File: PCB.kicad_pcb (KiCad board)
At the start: 2 copper layers, 60 x 60 mm, 56 parts, among them J1 USB_C_Receptacle_USB2.0_16P, J10 Conn_01x05_Pin, J11 Conn_01x05_Pin, J2 Conn_01x04_Pin, J3 Conn_01x04_Pin, J4 Conn_01x07_Pin, J5 Conn_01x02_Pin, J6 Conn_01x02_Pin, J7 Conn_01x02_Pin, J8 Conn_01x04_Pin, J9 Conn_01x07_Pin, SW1 SW_Push, SW2 SW_Push, U1 TMC2209_SILENTSTEPSTICK, U2 TMC2209_SILENTSTEPSTICK, U3 D3V3XA4B10LP, U4 AMS1117-3.3 (UMW), U5 TMC2209_SILENTSTEPSTICK, U6 ESP32-S3-WROOM-1

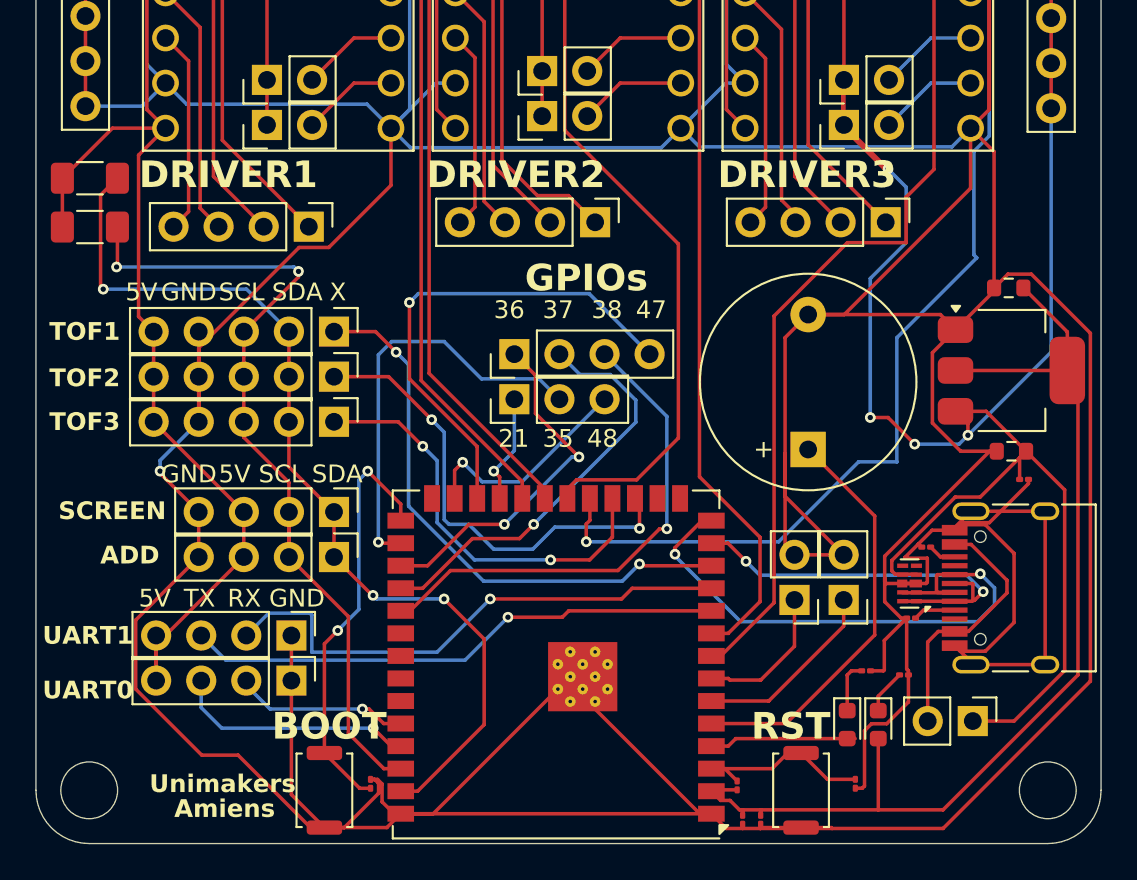
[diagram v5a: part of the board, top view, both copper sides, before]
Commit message: ajout hub 3.3v
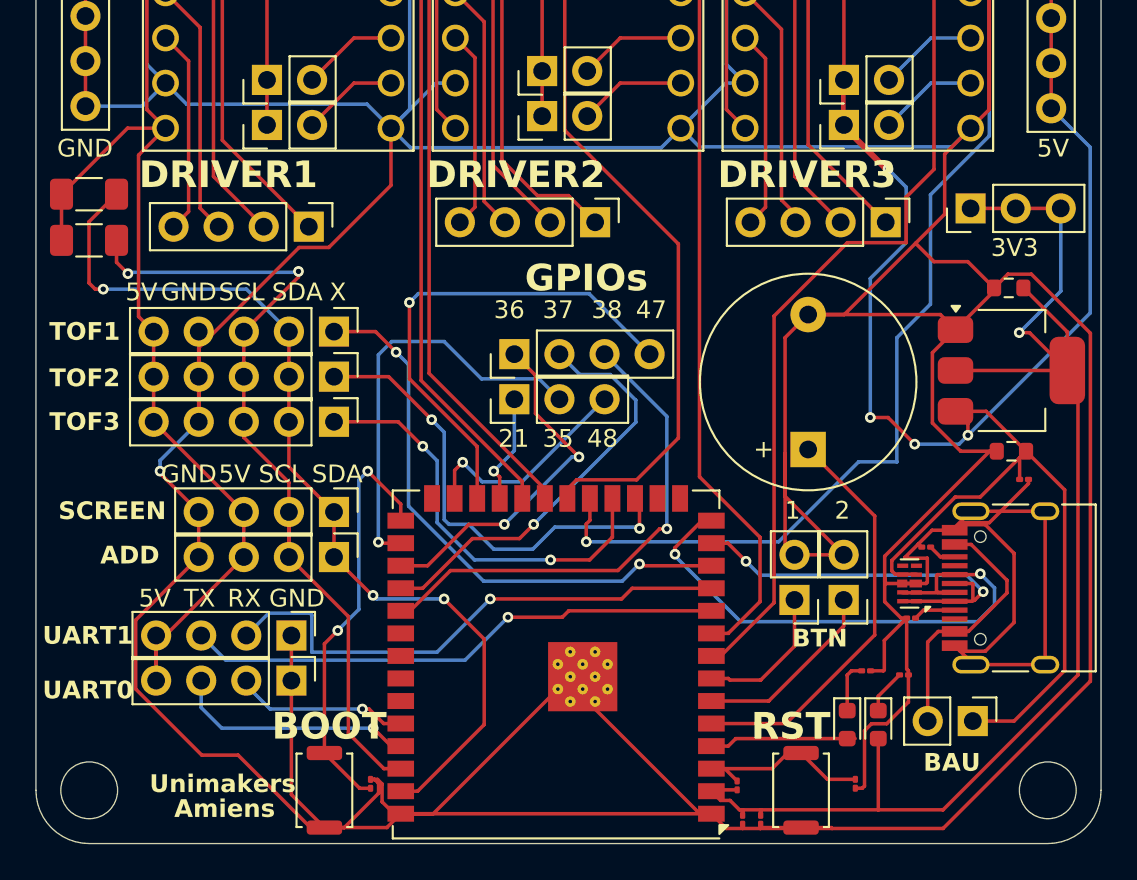
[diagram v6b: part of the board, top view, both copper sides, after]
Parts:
- added J12: Conn_01x03_Pin, Connector_PinHeader_2.54mm:PinHeader_1x03_P2.54mm_Vertical, F.Cu at (162.9, 97.2)
- moved JP8 0.90 mm to (113.2, 96.4)
- moved JP7 0.75 mm to (113.2, 99.0)
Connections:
- J11 pad 1: GND -> unconnected-(J11-Pin_1-Pad1)
- J11 pad 2: GND -> unconnected-(J11-Pin_2-Pad2)
- J11 pad 3: GND -> unconnected-(J11-Pin_3-Pad3)
- J11 pad 4: GND -> unconnected-(J11-Pin_4-Pad4)
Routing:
- net 3V3: track 59.7 -> 76.4 mm, vias 0 -> 1
- net GND: track 583.1 -> 579.0 mm
- net VCC_5V: track 323.5 -> 325.6 mm
- net SCL: track 48.7 -> 47.8 mm
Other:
- board text added: "1"
- board text added: "2"
- board text added: "3V3"
- board text added: "BAU"
- board text added: "BTN"

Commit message: Dernier DRC après modicifications
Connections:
- J11 pad 1: unconnected-(J11-Pin_1-Pad1) -> GND
- J11 pad 2: unconnected-(J11-Pin_2-Pad2) -> GND
- J11 pad 3: unconnected-(J11-Pin_3-Pad3) -> GND
- J11 pad 4: unconnected-(J11-Pin_4-Pad4) -> GND
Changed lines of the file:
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@@
 	(net 75 "MOTORC3")
 	(net 76 "MOTORC2")
-	(net 77 "unconnected-(J11-Pin_4-Pad4)")
-	(net 78 "unconnected-(J11-Pin_3-Pad3)")
-	(net 79 "unconnected-(J11-Pin_1-Pad1)")
-	(net 80 "unconnected-(J11-Pin_2-Pad2)")
 	(footprint "Buzzer_Beeper:Buzzer_12x9.5RM7.6"
 		(layer "F.Cu")
@@
 			(layers "*.Cu" "*.Mask")
 			(remove_unused_layers no)
-			(net 79 "unconnected-(J11-Pin_1-Pad1)")
+			(net 64 "GND")
 			(pinfunction "Pin_1")
 			(pintype "passive")
@@
 			(layers "*.Cu" "*.Mask")
 			(remove_unused_layers no)
-			(net 80 "unconnected-(J11-Pin_2-Pad2)")
+			(net 64 "GND")
 			(pinfunction "Pin_2")
 			(pintype "passive")
@@
 			(layers "*.Cu" "*.Mask")
 			(remove_unused_layers no)
-			(net 78 "unconnected-(J11-Pin_3-Pad3)")
+			(net 64 "GND")
 			(pinfunction "Pin_3")
 			(pintype "passive")
@@
 			(layers "*.Cu" "*.Mask")
 			(remove_unused_layers no)
-			(net 77 "unconnected-(J11-Pin_4-Pad4)")
+			(net 64 "GND")
 			(pinfunction "Pin_4")
 			(pintype "passive")

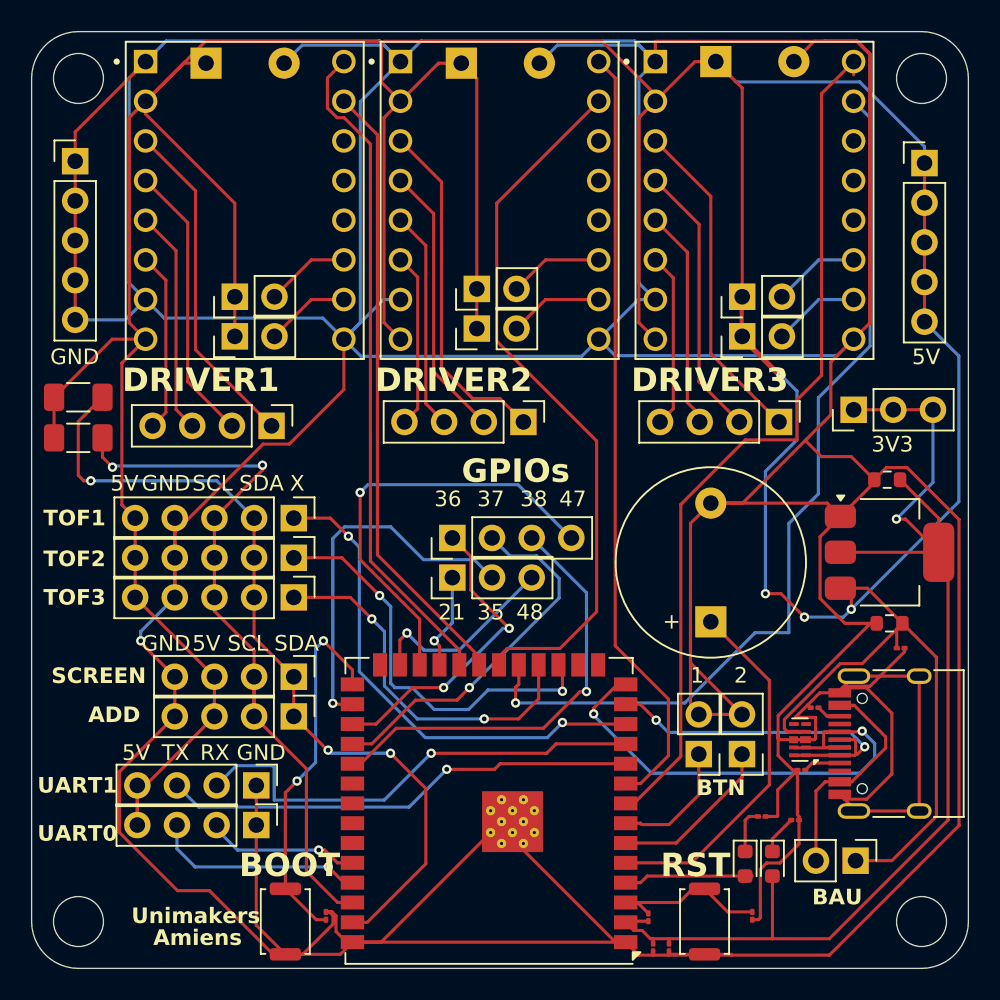
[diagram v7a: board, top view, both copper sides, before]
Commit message: ajout plan de masse
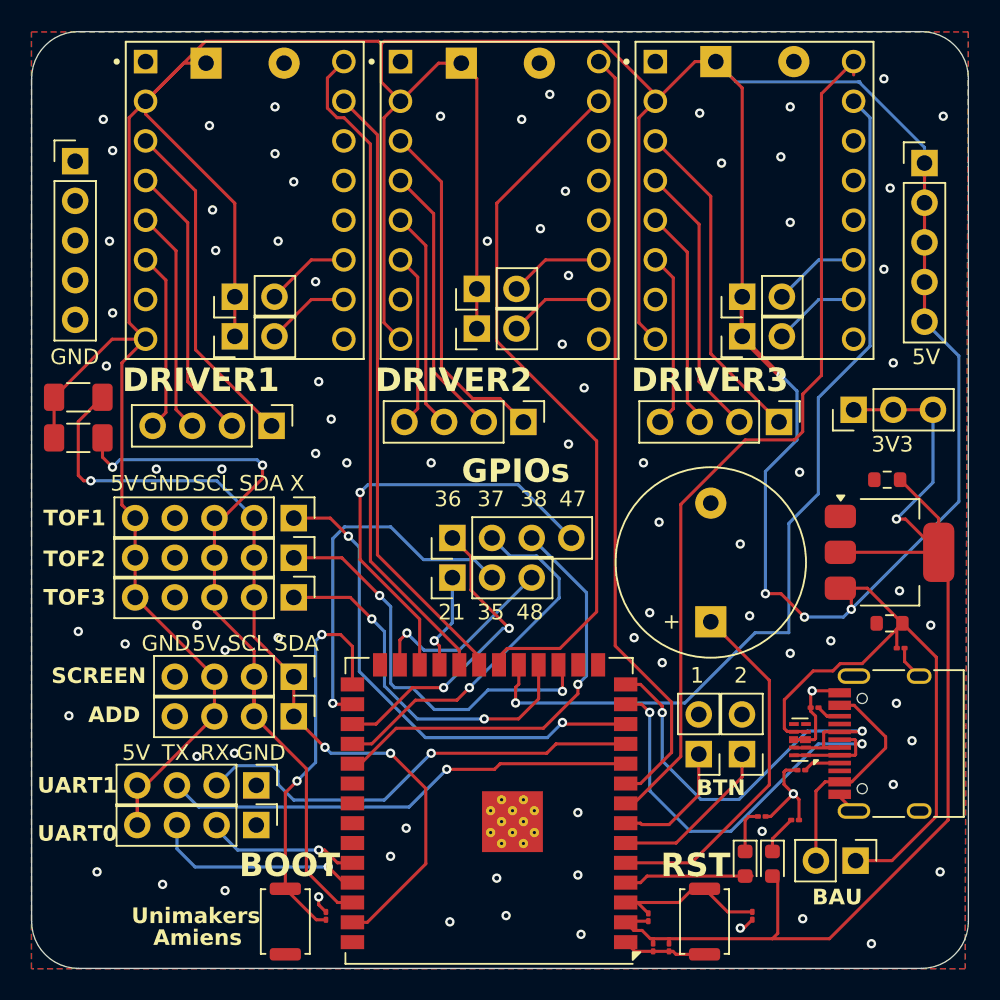
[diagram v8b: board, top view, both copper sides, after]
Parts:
- removed H1, H2, H3, H4: MountingHole, MountingHole:MountingHole_3.2mm_M3
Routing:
- net GND: track 579.0 -> 24.4 mm, vias 1 -> 82
- net USB_N: track 23.2 -> 30.1 mm
- net USB_P: track 32.8 -> 30.0 mm
- net GPIO0: track 23.9 -> 25.4 mm
- net VCC_5V: track 325.6 -> 326.4 mm
- net RX1: track 30.3 -> 29.6 mm
- net SCL: track 47.8 -> 48.5 mm
- added copper zone on B.Cu, net GND
- added copper zone on F.Cu, net GND
